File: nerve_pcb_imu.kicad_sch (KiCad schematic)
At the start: 14 parts, among them Y3 8M

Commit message: Update schematics
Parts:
- removed R18: 0R, Resistor_SMD:R_0603_1608Metric, symbol Device:R
- removed Y3: 8M, common:xtal_abm3b-8.000mhz-10-1-u-t, symbol common:abm3b-8.000mhz-10-1-u-t
- added R19, R20: 0R, Resistor_SMD:R_0402_1005Metric, symbol Device:R
- added Y3: 32k768, common:xtal_abs25-32.768khz-6-t, symbol common:abs25-32.768khz-6-t
- C16, C17: footprint Capacitor_SMD:C_0603_1608Metric -> Capacitor_SMD:C_0402_1005Metric
- C18, C19: value 20p -> 1p5; footprint Capacitor_SMD:C_0603_1608Metric -> Capacitor_SMD:C_0402_1005Metric
- C20: footprint (none) -> Capacitor_SMD:C_0402_1005Metric
- JP1: footprint (none) -> Jumper:SolderJumper-2_P1.3mm_Open_TrianglePad1.0x1.5mm
- R15, R16, R17: footprint (none) -> Resistor_SMD:R_0402_1005Metric
- R18: renamed from R19; footprint (none) -> Resistor_SMD:R_0402_1005Metric
- R21: renamed from R20; footprint (none) -> Resistor_SMD:R_0402_1005Metric
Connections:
- net at C19.1: now also R20.2, Y3.2; no longer U5.26 (XOUT32/CLKSEL1)
- net at U5.27 (XIN32): now also R19.1
- net at C18.1: now also R19.2, Y3.1
- new net: R20.1, U5.26 (XOUT32/CLKSEL1)

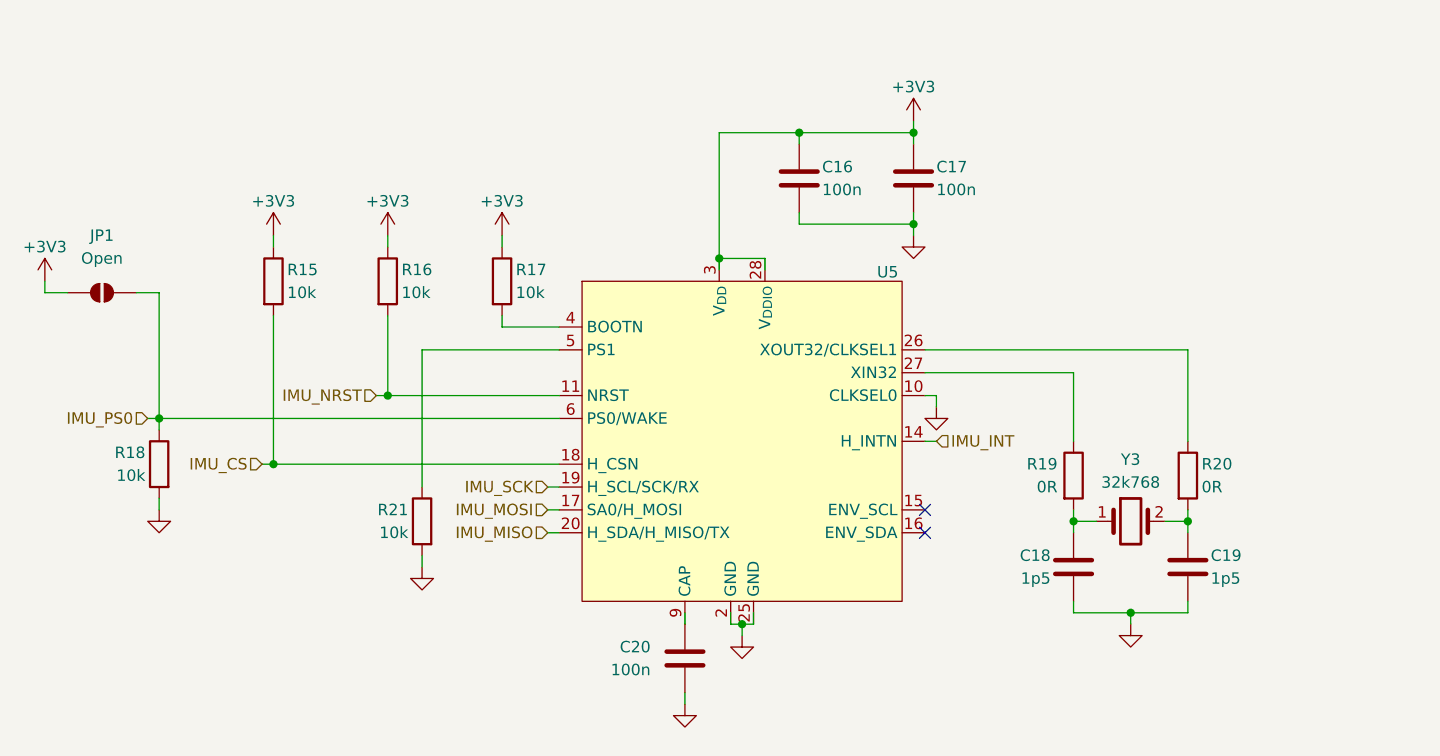
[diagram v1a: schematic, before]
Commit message: Add schematic changes from PCB routing/layout
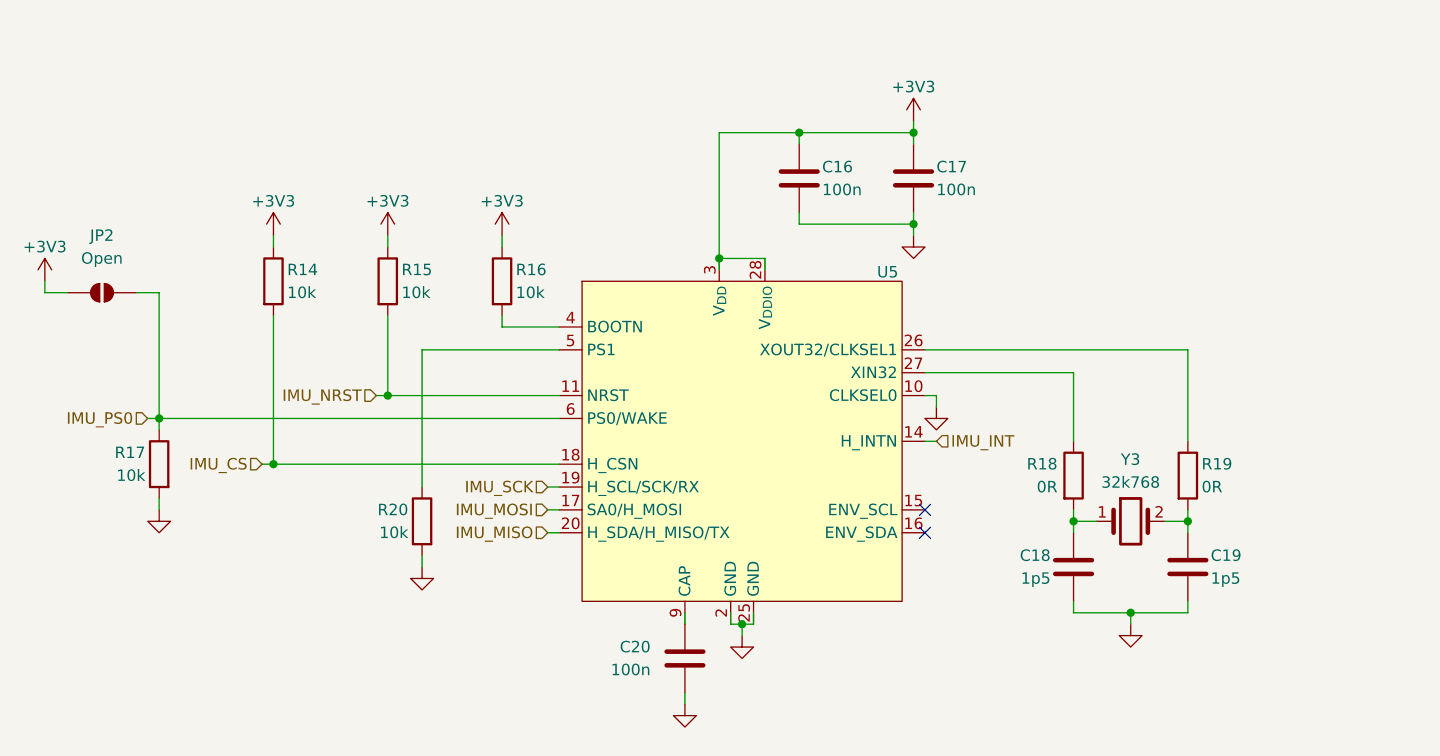
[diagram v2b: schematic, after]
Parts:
- renumbered JP1 to JP2, R15 to R14, R16 to R15, R17 to R16, R18 to R17, R19 to R18, R20 to R19, R21 to R20
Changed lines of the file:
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@@
 		(on_board yes)
 		(dnp no)
-		(property "Reference" "#PWR049"
+		(property "Reference" "#PWR047"
 			(at 82.55 91.44 0)
 			(effects
@@
 			(project "nerve_pcb"
 				(path "/c0277862-b3f2-4e0e-986f-34702f0543f0/1178a2c5-f6af-4893-bc81-c8b9cb81f032"
-					(reference "#PWR049")
+					(reference "#PWR047")
 					(unit 1)
 				)
@@
 		(dnp no)
 		(fields_autoplaced yes)
-		(property "Reference" "#PWR055"
+		(property "Reference" "#PWR053"
 			(at 153.67 140.97 0)
 			(effects
@@
 			(project "nerve_pcb"
 				(path "/c0277862-b3f2-4e0e-986f-34702f0543f0/1178a2c5-f6af-4893-bc81-c8b9cb81f032"
-					(reference "#PWR055")
+					(reference "#PWR053")
 					(unit 1)
 				)
@@
 		(dnp no)
 		(fields_autoplaced yes)
-		(property "Reference" "#PWR052"
+		(property "Reference" "#PWR050"
 			(at 124.46 125.73 0)
 			(effects
@@
 			(project "nerve_pcb"
 				(path "/c0277862-b3f2-4e0e-986f-34702f0543f0/1178a2c5-f6af-4893-bc81-c8b9cb81f032"
-					(reference "#PWR052")
+					(reference "#PWR050")
 					(unit 1)
 				)
@@
 		(dnp no)
 		(fields_autoplaced yes)
-		(property "Reference" "#PWR051"
+		(property "Reference" "#PWR049"
 			(at 95.25 119.38 0)
 			(effects
@@
 			(project "nerve_pcb"
 				(path "/c0277862-b3f2-4e0e-986f-34702f0543f0/1178a2c5-f6af-4893-bc81-c8b9cb81f032"
-					(reference "#PWR051")
+					(reference "#PWR049")
 					(unit 1)
 				)
@@
 		(on_board yes)
 		(dnp no)
-		(property "Reference" "R20"
+		(property "Reference" "R19"
 			(at 211.074 107.95 0)
 			(effects
@@
 			(project "nerve_pcb"
 				(path "/c0277862-b3f2-4e0e-986f-34702f0543f0/1178a2c5-f6af-4893-bc81-c8b9cb81f032"
-					(reference "R20")
+					(reference "R19")
 					(unit 1)
 				)
@@
 		(dnp no)
 		(fields_autoplaced yes)
-		(property "Reference" "JP1"
+		(property "Reference" "JP2"
 			(at 88.9 82.55 0)
 			(effects
@@
 			(project ""
 				(path "/c0277862-b3f2-4e0e-986f-34702f0543f0/1178a2c5-f6af-4893-bc81-c8b9cb81f032"
-					(reference "JP1")
+					(reference "JP2")
 					(unit 1)
 				)
@@
 		(on_board yes)
 		(dnp no)
-		(property "Reference" "R18"
+		(property "Reference" "R17"
 			(at 93.726 106.68 0)
 			(effects
@@
 			(project "nerve_pcb"
 				(path "/c0277862-b3f2-4e0e-986f-34702f0543f0/1178a2c5-f6af-4893-bc81-c8b9cb81f032"
-					(reference "R18")
+					(reference "R17")
 					(unit 1)
 				)
@@
 		(on_board yes)
 		(dnp no)
-		(property "Reference" "#PWR046"
+		(property "Reference" "#PWR044"
 			(at 120.65 86.36 0)
 			(effects
@@
 			(project "nerve_pcb"
 				(path "/c0277862-b3f2-4e0e-986f-34702f0543f0/1178a2c5-f6af-4893-bc81-c8b9cb81f032"
-					(reference "#PWR046")
+					(reference "#PWR044")
 					(unit 1)
 				)
@@
 		(on_board yes)
 		(dnp no)
-		(property "Reference" "R21"
+		(property "Reference" "R20"
 			(at 122.936 113.03 0)
 			(effects
@@
 			(project "nerve_pcb"
 				(path "/c0277862-b3f2-4e0e-986f-34702f0543f0/1178a2c5-f6af-4893-bc81-c8b9cb81f032"
-					(reference "R21")
+					(reference "R20")
 					(unit 1)
 				)
@@
 		(dnp no)
 		(fields_autoplaced yes)
-		(property "Reference" "#PWR054"
+		(property "Reference" "#PWR052"
 			(at 160.02 133.35 0)
 			(effects
@@
 			(project "nerve_pcb"
 				(path "/c0277862-b3f2-4e0e-986f-34702f0543f0/1178a2c5-f6af-4893-bc81-c8b9cb81f032"
-					(reference "#PWR054")
+					(reference "#PWR052")
 					(unit 1)
 				)
@@
 		(dnp no)
 		(fields_autoplaced yes)
-		(property "Reference" "#PWR048"
+		(property "Reference" "#PWR046"
 			(at 179.07 88.9 0)
 			(effects
@@
 			(project "nerve_pcb"
 				(path "/c0277862-b3f2-4e0e-986f-34702f0543f0/1178a2c5-f6af-4893-bc81-c8b9cb81f032"
-					(reference "#PWR048")
+					(reference "#PWR046")
 					(unit 1)
 				)
@@
 		(on_board yes)
 		(dnp no)
-		(property "Reference" "#PWR047"
+		(property "Reference" "#PWR045"
 			(at 133.35 86.36 0)
 			(effects
@@
 			(project "nerve_pcb"
 				(path "/c0277862-b3f2-4e0e-986f-34702f0543f0/1178a2c5-f6af-4893-bc81-c8b9cb81f032"
-					(reference "#PWR047")
+					(reference "#PWR045")
 					(unit 1)
 				)
@@
 		(dnp no)
 		(fields_autoplaced yes)
-		(property "Reference" "#PWR053"
+		(property "Reference" "#PWR051"
 			(at 203.2 132.08 0)
 			(effects
@@
 			(project "nerve_pcb"
 				(path "/c0277862-b3f2-4e0e-986f-34702f0543f0/1178a2c5-f6af-4893-bc81-c8b9cb81f032"
-					(reference "#PWR053")
+					(reference "#PWR051")
 					(unit 1)
 				)
@@
 		(on_board yes)
 		(dnp no)
-		(property "Reference" "R16"
+		(property "Reference" "R15"
 			(at 122.174 86.36 0)
 			(effects
@@
 			(project "nerve_pcb"
 				(path "/c0277862-b3f2-4e0e-986f-34702f0543f0/1178a2c5-f6af-4893-bc81-c8b9cb81f032"
-					(reference "R16")
+					(reference "R15")
 					(unit 1)
 				)
@@
 		(on_board yes)
 		(dnp no)
-		(property "Reference" "R15"
+		(property "Reference" "R14"
 			(at 109.474 86.36 0)
 			(effects
@@
 			(project "nerve_pcb"
 				(path "/c0277862-b3f2-4e0e-986f-34702f0543f0/1178a2c5-f6af-4893-bc81-c8b9cb81f032"
-					(reference "R15")
+					(reference "R14")
 					(unit 1)
 				)
@@
 		(on_board yes)
 		(dnp no)
-		(property "Reference" "R17"
+		(property "Reference" "R16"
 			(at 134.874 86.36 0)
 			(effects
@@
 			(project "nerve_pcb"
 				(path "/c0277862-b3f2-4e0e-986f-34702f0543f0/1178a2c5-f6af-4893-bc81-c8b9cb81f032"
-					(reference "R17")
+					(reference "R16")
 					(unit 1)
 				)
@@
 		(dnp no)
 		(fields_autoplaced yes)
-		(property "Reference" "#PWR050"
+		(property "Reference" "#PWR048"
 			(at 181.61 107.95 0)
 			(effects
@@
 			(project "nerve_pcb"
 				(path "/c0277862-b3f2-4e0e-986f-34702f0543f0/1178a2c5-f6af-4893-bc81-c8b9cb81f032"
-					(reference "#PWR050")
+					(reference "#PWR048")
 					(unit 1)
 				)
@@
 		(on_board yes)
 		(dnp no)
-		(property "Reference" "#PWR045"
+		(property "Reference" "#PWR043"
 			(at 107.95 86.36 0)
 			(effects
@@
 			(project "nerve_pcb"
 				(path "/c0277862-b3f2-4e0e-986f-34702f0543f0/1178a2c5-f6af-4893-bc81-c8b9cb81f032"
-					(reference "#PWR045")
+					(reference "#PWR043")
 					(unit 1)
 				)
@@
 		(on_board yes)
 		(dnp no)
-		(property "Reference" "#PWR044"
+		(property "Reference" "#PWR042"
 			(at 179.07 73.66 0)
 			(effects
@@
 			(project "nerve_pcb"
 				(path "/c0277862-b3f2-4e0e-986f-34702f0543f0/1178a2c5-f6af-4893-bc81-c8b9cb81f032"
-					(reference "#PWR044")
+					(reference "#PWR042")
 					(unit 1)
 				)
@@
 		(on_board yes)
 		(dnp no)
-		(property "Reference" "R19"
+		(property "Reference" "R18"
 			(at 195.072 107.95 0)
 			(effects
@@
 			(project "nerve_pcb"
 				(path "/c0277862-b3f2-4e0e-986f-34702f0543f0/1178a2c5-f6af-4893-bc81-c8b9cb81f032"
-					(reference "R19")
-					(unit 1)
-				)
+					(reference "R18")
+					(unit 1)
+				)

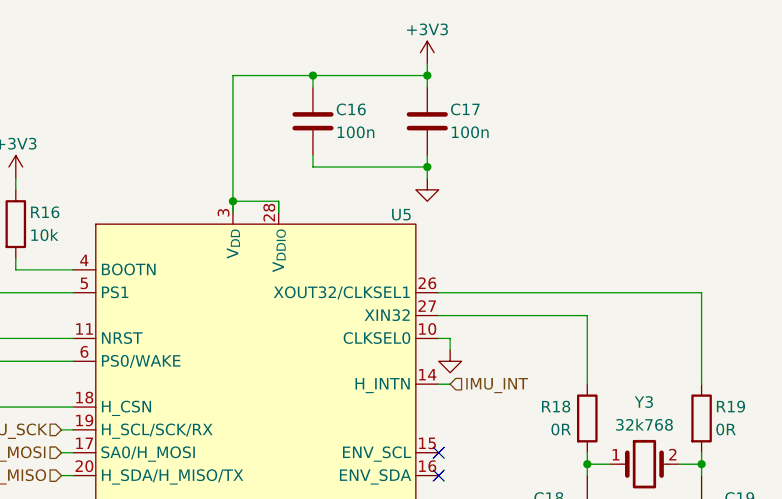
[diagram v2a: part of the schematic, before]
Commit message: Update refs on schematics
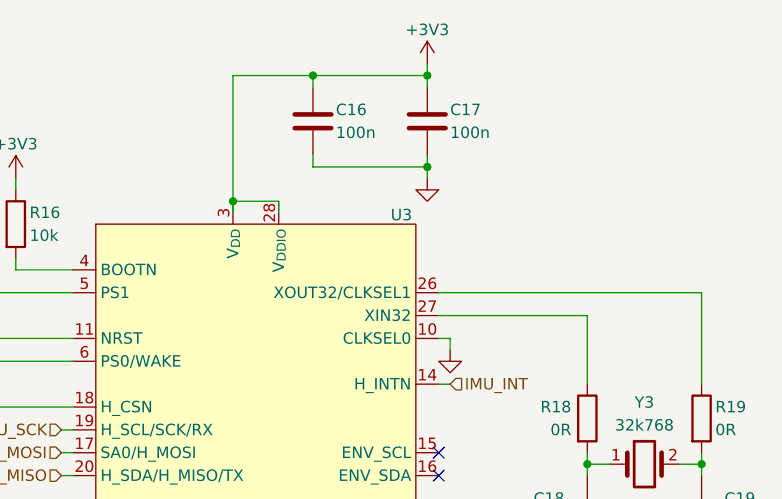
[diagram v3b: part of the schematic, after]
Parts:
- renumbered U5 to U3
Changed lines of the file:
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@@
 		(on_board yes)
 		(dnp no)
-		(property "Reference" "#PWR047"
+		(property "Reference" "#PWR063"
 			(at 82.55 91.44 0)
 			(effects
@@
 			(project "nerve_pcb"
 				(path "/c0277862-b3f2-4e0e-986f-34702f0543f0/1178a2c5-f6af-4893-bc81-c8b9cb81f032"
-					(reference "#PWR047")
+					(reference "#PWR063")
 					(unit 1)
 				)
@@
 		(dnp no)
 		(fields_autoplaced yes)
-		(property "Reference" "#PWR053"
+		(property "Reference" "#PWR069"
 			(at 153.67 140.97 0)
 			(effects
@@
 			(project "nerve_pcb"
 				(path "/c0277862-b3f2-4e0e-986f-34702f0543f0/1178a2c5-f6af-4893-bc81-c8b9cb81f032"
-					(reference "#PWR053")
+					(reference "#PWR069")
 					(unit 1)
 				)
@@
 		(dnp no)
 		(fields_autoplaced yes)
-		(property "Reference" "#PWR050"
+		(property "Reference" "#PWR066"
 			(at 124.46 125.73 0)
 			(effects
@@
 			(project "nerve_pcb"
 				(path "/c0277862-b3f2-4e0e-986f-34702f0543f0/1178a2c5-f6af-4893-bc81-c8b9cb81f032"
-					(reference "#PWR050")
+					(reference "#PWR066")
 					(unit 1)
 				)
@@
 		(dnp no)
 		(fields_autoplaced yes)
-		(property "Reference" "#PWR049"
+		(property "Reference" "#PWR065"
 			(at 95.25 119.38 0)
 			(effects
@@
 			(project "nerve_pcb"
 				(path "/c0277862-b3f2-4e0e-986f-34702f0543f0/1178a2c5-f6af-4893-bc81-c8b9cb81f032"
-					(reference "#PWR049")
+					(reference "#PWR065")
 					(unit 1)
 				)
@@
 		(on_board yes)
 		(dnp no)
-		(property "Reference" "U5"
+		(property "Reference" "U3"
 			(at 175.006 86.614 0)
 			(effects
@@
 			(project ""
 				(path "/c0277862-b3f2-4e0e-986f-34702f0543f0/1178a2c5-f6af-4893-bc81-c8b9cb81f032"
-					(reference "U5")
+					(reference "U3")
 					(unit 1)
 				)
@@
 		(on_board yes)
 		(dnp no)
-		(property "Reference" "#PWR044"
+		(property "Reference" "#PWR060"
 			(at 120.65 86.36 0)
 			(effects
@@
 			(project "nerve_pcb"
 				(path "/c0277862-b3f2-4e0e-986f-34702f0543f0/1178a2c5-f6af-4893-bc81-c8b9cb81f032"
-					(reference "#PWR044")
+					(reference "#PWR060")
 					(unit 1)
 				)
@@
 		(dnp no)
 		(fields_autoplaced yes)
-		(property "Reference" "#PWR052"
+		(property "Reference" "#PWR068"
 			(at 160.02 133.35 0)
 			(effects
@@
 			(project "nerve_pcb"
 				(path "/c0277862-b3f2-4e0e-986f-34702f0543f0/1178a2c5-f6af-4893-bc81-c8b9cb81f032"
-					(reference "#PWR052")
+					(reference "#PWR068")
 					(unit 1)
 				)
@@
 		(dnp no)
 		(fields_autoplaced yes)
-		(property "Reference" "#PWR046"
+		(property "Reference" "#PWR062"
 			(at 179.07 88.9 0)
 			(effects
@@
 			(project "nerve_pcb"
 				(path "/c0277862-b3f2-4e0e-986f-34702f0543f0/1178a2c5-f6af-4893-bc81-c8b9cb81f032"
-					(reference "#PWR046")
+					(reference "#PWR062")
 					(unit 1)
 				)
@@
 		(on_board yes)
 		(dnp no)
-		(property "Reference" "#PWR045"
+		(property "Reference" "#PWR061"
 			(at 133.35 86.36 0)
 			(effects
@@
 			(project "nerve_pcb"
 				(path "/c0277862-b3f2-4e0e-986f-34702f0543f0/1178a2c5-f6af-4893-bc81-c8b9cb81f032"
-					(reference "#PWR045")
+					(reference "#PWR061")
 					(unit 1)
 				)
@@
 		(dnp no)
 		(fields_autoplaced yes)
-		(property "Reference" "#PWR051"
+		(property "Reference" "#PWR067"
 			(at 203.2 132.08 0)
 			(effects
@@
 			(project "nerve_pcb"
 				(path "/c0277862-b3f2-4e0e-986f-34702f0543f0/1178a2c5-f6af-4893-bc81-c8b9cb81f032"
-					(reference "#PWR051")
+					(reference "#PWR067")
 					(unit 1)
 				)
@@
 		(dnp no)
 		(fields_autoplaced yes)
-		(property "Reference" "#PWR048"
+		(property "Reference" "#PWR064"
 			(at 181.61 107.95 0)
 			(effects
@@
 			(project "nerve_pcb"
 				(path "/c0277862-b3f2-4e0e-986f-34702f0543f0/1178a2c5-f6af-4893-bc81-c8b9cb81f032"
-					(reference "#PWR048")
+					(reference "#PWR064")
 					(unit 1)
 				)
@@
 		(on_board yes)
 		(dnp no)
-		(property "Reference" "#PWR043"
+		(property "Reference" "#PWR059"
 			(at 107.95 86.36 0)
 			(effects
@@
 			(project "nerve_pcb"
 				(path "/c0277862-b3f2-4e0e-986f-34702f0543f0/1178a2c5-f6af-4893-bc81-c8b9cb81f032"
-					(reference "#PWR043")
+					(reference "#PWR059")
 					(unit 1)
 				)
@@
 		(on_board yes)
 		(dnp no)
-		(property "Reference" "#PWR042"
+		(property "Reference" "#PWR058"
 			(at 179.07 73.66 0)
 			(effects
@@
 			(project "nerve_pcb"
 				(path "/c0277862-b3f2-4e0e-986f-34702f0543f0/1178a2c5-f6af-4893-bc81-c8b9cb81f032"
-					(reference "#PWR042")
-					(unit 1)
-				)
+					(reference "#PWR058")
+					(unit 1)
+				)
